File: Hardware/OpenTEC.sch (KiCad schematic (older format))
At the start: 65 parts, among them J10 TEMP3, J11 TEC, J12 XH2.54, J13 XH2.54, J14 XH2.54, J15 XH2.54, J16 XH2.54, J17 XH2.54, J18 XH2.54, J19 XH2.54, J2 4P Screw Terminal, J20 XH2.54, J21 XH2.54, J22 XH2.54, J23 XH2.54, J24 XH2.54, J25 XH2.54, J26 XH2.54, J27 XH2.54, J3 10P JTAG/SWD, J4 LCD, J5 I2C, J6 BOOT_SEL, J7 TEMP0, J8 TEMP1, J9 TEMP2, Q1 FDS6574A, Q2 FDS6574A, Q3 FDS6574A, Q4 FDS6574A, U11 STM32F103C8T6, U2 AMS1117-3.3, U3 IR2104, U4 IR2104, Y1 16MHz

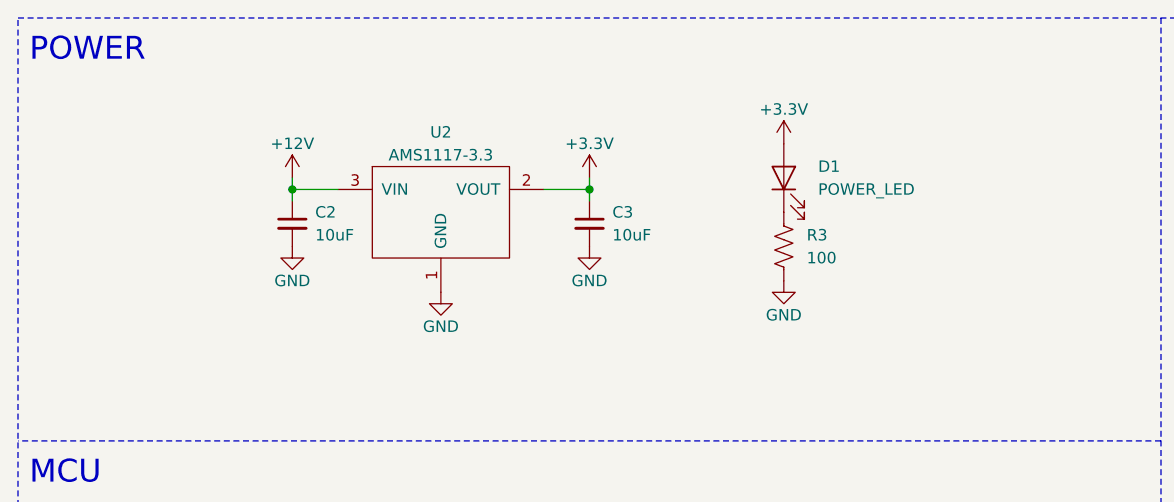
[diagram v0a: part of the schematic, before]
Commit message: Add RC filter to 3.3V LDO input
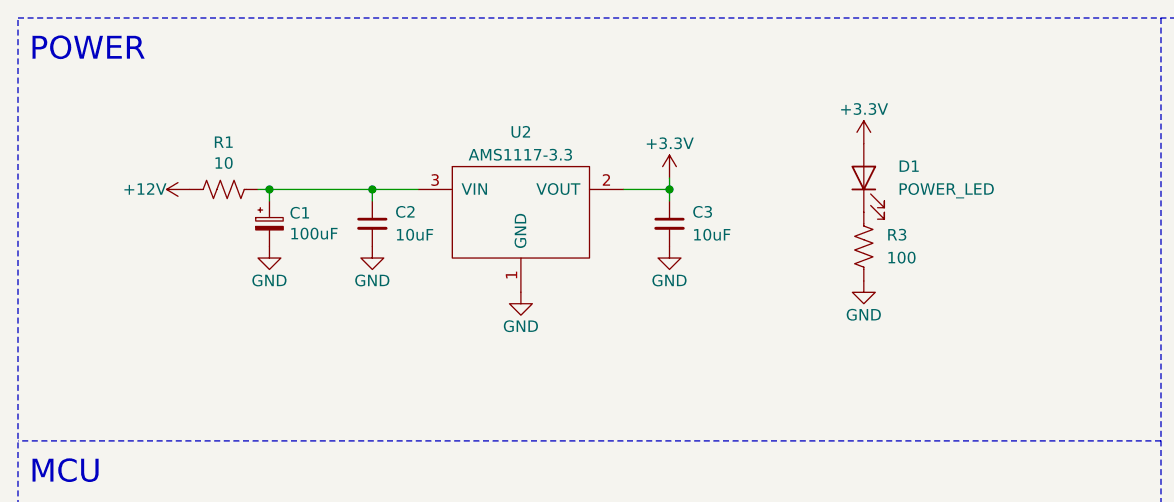
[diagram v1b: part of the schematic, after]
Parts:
- added C1: 100uF, Capacitor_SMD:CP_Elec_6.3x5.8, symbol Device:CP_Small
- added R1: 10, Resistor_THT:R_Axial_Power_L20.0mm_W6.4mm_P22.40mm, symbol Device:R_US
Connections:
- net +12V: now also R1.2; no longer C2.1, U2.3 (VIN)
- net GND: now also C1.2
- new net: C1.1, C2.1, R1.1, U2.3 (VIN)
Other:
- moved on the sheet: C2, C3, D1, R3, U2
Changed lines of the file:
@@
 L power:+3.3V #PWR03
 U 1 1 6014EE85
-P 3850 1050
-F 0 "#PWR03" H 3850 900 50  0001 C CNN
-F 1 "+3.3V" H 3850 1200 50  0000 C CNN
-F 2 "" H 3850 1050 50  0001 C CNN
-F 3 "" H 3850 1050 50  0001 C CNN
-	1    3850 1050
+P 4200 1050
+F 0 "#PWR03" H 4200 900 50  0001 C CNN
+F 1 "+3.3V" H 4200 1200 50  0000 C CNN
+F 2 "" H 4200 1050 50  0001 C CNN
+F 3 "" H 4200 1050 50  0001 C CNN
+	1    4200 1050
 	1    0    0    -1
 $EndComp
@@
 L power:GND #PWR012
 U 1 1 6014DF95
-P 3850 1650
-F 0 "#PWR012" H 3850 1400 50  0001 C CNN
-F 1 "GND" H 3850 1500 50  0000 C CNN
-F 2 "" H 3850 1650 50  0001 C CNN
-F 3 "" H 3850 1650 50  0001 C CNN
-	1    3850 1650
+P 4200 1650
+F 0 "#PWR012" H 4200 1400 50  0001 C CNN
+F 1 "GND" H 4200 1500 50  0000 C CNN
+F 2 "" H 4200 1650 50  0001 C CNN
+F 3 "" H 4200 1650 50  0001 C CNN
+	1    4200 1650
 	1    0    0    -1
 $EndComp
@@
 L Device:R_US R3
 U 1 1 6014CE76
-P 3850 1500
-F 0 "R3" H 3950 1550 50  0000 L CNN
-F 1 "100" H 3950 1450 50  0000 L CNN
-F 2 "Resistor_SMD:R_0402_1005Metric" V 3890 1490 50  0001 C CNN
-F 3 "~" H 3850 1500 50  0001 C CNN
-	1    3850 1500
+P 4200 1500
+F 0 "R3" H 4300 1550 50  0000 L CNN
+F 1 "100" H 4300 1450 50  0000 L CNN
+F 2 "Resistor_SMD:R_0402_1005Metric" V 4240 1490 50  0001 C CNN
+F 3 "~" H 4200 1500 50  0001 C CNN
+	1    4200 1500
 	1    0    0    -1
 $EndComp
@@
 L Device:LED D1
 U 1 1 6014BC21
-P 3850 1200
-F 0 "D1" V 3900 1050 50  0000 R CNN
-F 1 "POWER_LED" V 3800 1050 50  0000 R CNN
-F 2 "LED_SMD:LED_0603_1608Metric" H 3850 1200 50  0001 C CNN
-F 3 "~" H 3850 1200 50  0001 C CNN
-	1    3850 1200
+P 4200 1200
+F 0 "D1" V 4250 1050 50  0000 R CNN
+F 1 "POWER_LED" V 4150 1050 50  0000 R CNN
+F 2 "LED_SMD:LED_0603_1608Metric" H 4200 1200 50  0001 C CNN
+F 3 "~" H 4200 1200 50  0001 C CNN
+	1    4200 1200
 	0    -1   -1   0
 $EndComp
-Wire Wire Line
-	1700 1200 1700 1250
-Connection ~ 3000 1250
-Wire Wire Line
-	3000 1200 3000 1250
-$Comp
-L power:+12V #PWR06
-U 1 1 6012AA6B
-P 1700 1200
-F 0 "#PWR06" H 1700 1050 50  0001 C CNN
-F 1 "+12V" H 1700 1350 50  0000 C CNN
-F 2 "" H 1700 1200 50  0001 C CNN
-F 3 "" H 1700 1200 50  0001 C CNN
-	1    1700 1200
-	1    0    0    -1
-$EndComp
+Connection ~ 3350 1250
+Wire Wire Line
+	3350 1200 3350 1250
 $Comp
 L power:+3.3V #PWR08
 U 1 1 601276ED
-P 3000 1200
-F 0 "#PWR08" H 3000 1050 50  0001 C CNN
-F 1 "+3.3V" H 3000 1350 50  0000 C CNN
-F 2 "" H 3000 1200 50  0001 C CNN
-F 3 "" H 3000 1200 50  0001 C CNN
-	1    3000 1200
+P 3350 1200
+F 0 "#PWR08" H 3350 1050 50  0001 C CNN
+F 1 "+3.3V" H 3350 1350 50  0000 C CNN
+F 2 "" H 3350 1200 50  0001 C CNN
+F 3 "" H 3350 1200 50  0001 C CNN
+	1    3350 1200
 	1    0    0    -1
 $EndComp
@@
 L power:GND #PWR014
 U 1 1 601272FB
-P 2350 1700
-F 0 "#PWR014" H 2350 1450 50  0001 C CNN
-F 1 "GND" H 2350 1550 50  0000 C CNN
-F 2 "" H 2350 1700 50  0001 C CNN
-F 3 "" H 2350 1700 50  0001 C CNN
-	1    2350 1700
-	1    0    0    -1
-$EndComp
-Wire Wire Line
-	3000 1250 3000 1300
-Wire Wire Line
-	2800 1250 3000 1250
-Wire Wire Line
-	1700 1250 1900 1250
-Connection ~ 1700 1250
-Wire Wire Line
-	1700 1300 1700 1250
+P 2700 1700
+F 0 "#PWR014" H 2700 1450 50  0001 C CNN
+F 1 "GND" H 2700 1550 50  0000 C CNN
+F 2 "" H 2700 1700 50  0001 C CNN
+F 3 "" H 2700 1700 50  0001 C CNN
+	1    2700 1700
+	1    0    0    -1
+$EndComp
+Wire Wire Line
+	3350 1250 3350 1300
+Wire Wire Line
+	3150 1250 3350 1250
+Wire Wire Line
+	2050 1250 2250 1250
+Wire Wire Line
+	2050 1300 2050 1250
 $Comp
 L power:GND #PWR011
 U 1 1 6012585B
-P 3000 1500
-F 0 "#PWR011" H 3000 1250 50  0001 C CNN
-F 1 "GND" H 3000 1350 50  0000 C CNN
-F 2 "" H 3000 1500 50  0001 C CNN
-F 3 "" H 3000 1500 50  0001 C CNN
-	1    3000 1500
+P 3350 1500
+F 0 "#PWR011" H 3350 1250 50  0001 C CNN
+F 1 "GND" H 3350 1350 50  0000 C CNN
+F 2 "" H 3350 1500 50  0001 C CNN
+F 3 "" H 3350 1500 50  0001 C CNN
+	1    3350 1500
 	1    0    0    -1
 $EndComp
@@
 L Device:C_Small C3
 U 1 1 60125855
-P 3000 1400
-F 0 "C3" H 3100 1450 50  0000 L CNN
-F 1 "10uF" H 3100 1350 50  0000 L CNN
-F 2 "Capacitor_SMD:C_0805_2012Metric" H 3000 1400 50  0001 C CNN
-F 3 "~" H 3000 1400 50  0001 C CNN
-	1    3000 1400
+P 3350 1400
+F 0 "C3" H 3450 1450 50  0000 L CNN
+F 1 "10uF" H 3450 1350 50  0000 L CNN
+F 2 "Capacitor_SMD:C_0805_2012Metric" H 3350 1400 50  0001 C CNN
+F 3 "~" H 3350 1400 50  0001 C CNN
+	1    3350 1400
 	1    0    0    -1
 $EndComp
@@
 L power:GND #PWR010
 U 1 1 6012438B
-P 1700 1500
-F 0 "#PWR010" H 1700 1250 50  0001 C CNN
-F 1 "GND" H 1700 1350 50  0000 C CNN
-F 2 "" H 1700 1500 50  0001 C CNN
-F 3 "" H 1700 1500 50  0001 C CNN
-	1    1700 1500
+P 2050 1500
+F 0 "#PWR010" H 2050 1250 50  0001 C CNN
+F 1 "GND" H 2050 1350 50  0000 C CNN
+F 2 "" H 2050 1500 50  0001 C CNN
+F 3 "" H 2050 1500 50  0001 C CNN
+	1    2050 1500
 	1    0    0    -1
 $EndComp
@@
 L Device:C_Small C2
 U 1 1 60124385
-P 1700 1400
-F 0 "C2" H 1800 1450 50  0000 L CNN
-F 1 "10uF" H 1800 1350 50  0000 L CNN
-F 2 "Capacitor_SMD:C_0805_2012Metric" H 1700 1400 50  0001 C CNN
-F 3 "~" H 1700 1400 50  0001 C CNN
-	1    1700 1400
+P 2050 1400
+F 0 "C2" H 2150 1450 50  0000 L CNN
+F 1 "10uF" H 2150 1350 50  0000 L CNN
+F 2 "Capacitor_SMD:C_0805_2012Metric" H 2050 1400 50  0001 C CNN
+F 3 "~" H 2050 1400 50  0001 C CNN
+	1    2050 1400
 	1    0    0    -1
 $EndComp
@@
 L OpenTEC:AMS1117 U2
 U 1 1 6011CBE4
-P 2350 1300
-F 0 "U2" H 2350 1600 50  0000 C CNN
-F 1 "AMS1117-3.3" H 2350 1500 50  0000 C CNN
-F 2 "Package_TO_SOT_SMD:SOT-223-3_TabPin2" H 2350 1600 50  0001 C CNN
-F 3 "" H 2350 1600 50  0001 C CNN
-	1    2350 1300
+P 2700 1300
+F 0 "U2" H 2700 1600 50  0000 C CNN
+F 1 "AMS1117-3.3" H 2700 1500 50  0000 C CNN
+F 2 "Package_TO_SOT_SMD:SOT-223-3_TabPin2" H 2700 1600 50  0001 C CNN
+F 3 "" H 2700 1600 50  0001 C CNN
+	1    2700 1300
 	1    0    0    -1
 $EndComp
@@
 NoConn ~ 2650 6250
 NoConn ~ 2650 6350
+$Comp
+L Device:R_US R1
+U 1 1 601B9489
+P 1400 1250
+F 0 "R1" V 1195 1250 50  0000 C CNN
+F 1 "10" V 1286 1250 50  0000 C CNN
+F 2 "Resistor_THT:R_Axial_Power_L20.0mm_W6.4mm_P22.40mm" V 1440 1240 50  0001 C CNN
+F 3 "~" H 1400 1250 50  0001 C CNN
+	1    1400 1250
+	0    1    1    0
+$EndComp
+$Comp
+L power:+12V #PWR02
+U 1 1 601BC96C
+P 1250 1250
+F 0 "#PWR02" H 1250 1100 50  0001 C CNN
+F 1 "+12V" V 1250 1350 50  0000 L CNN
+F 2 "" H 1250 1250 50  0001 C CNN
+F 3 "" H 1250 1250 50  0001 C CNN
+	1    1250 1250
+	0    -1   -1   0
+$EndComp
+$Comp
+L power:GND #PWR05
+U 1 1 601C1543
+P 1600 1500
+F 0 "#PWR05" H 1600 1250 50  0001 C CNN
+F 1 "GND" H 1600 1350 50  0000 C CNN
+F 2 "" H 1600 1500 50  0001 C CNN
+F 3 "" H 1600 1500 50  0001 C CNN
+	1    1600 1500
+	1    0    0    -1
+$EndComp
+$Comp
+L Device:CP_Small C1
+U 1 1 601C37E4
+P 1600 1400
+F 0 "C1" H 1688 1446 50  0000 L CNN
+F 1 "100uF" H 1688 1355 50  0000 L CNN
+F 2 "Capacitor_SMD:CP_Elec_6.3x5.8" H 1600 1400 50  0001 C CNN
+F 3 "~" H 1600 1400 50  0001 C CNN
+	1    1600 1400
+	1    0    0    -1
+$EndComp
+Wire Wire Line
+	1600 1250 1550 1250
+Wire Wire Line
+	1600 1250 1600 1300
+Connection ~ 1600 1250
+Wire Wire Line
+	1600 1250 2050 1250
+Connection ~ 2050 1250
 $EndSCHEMATC

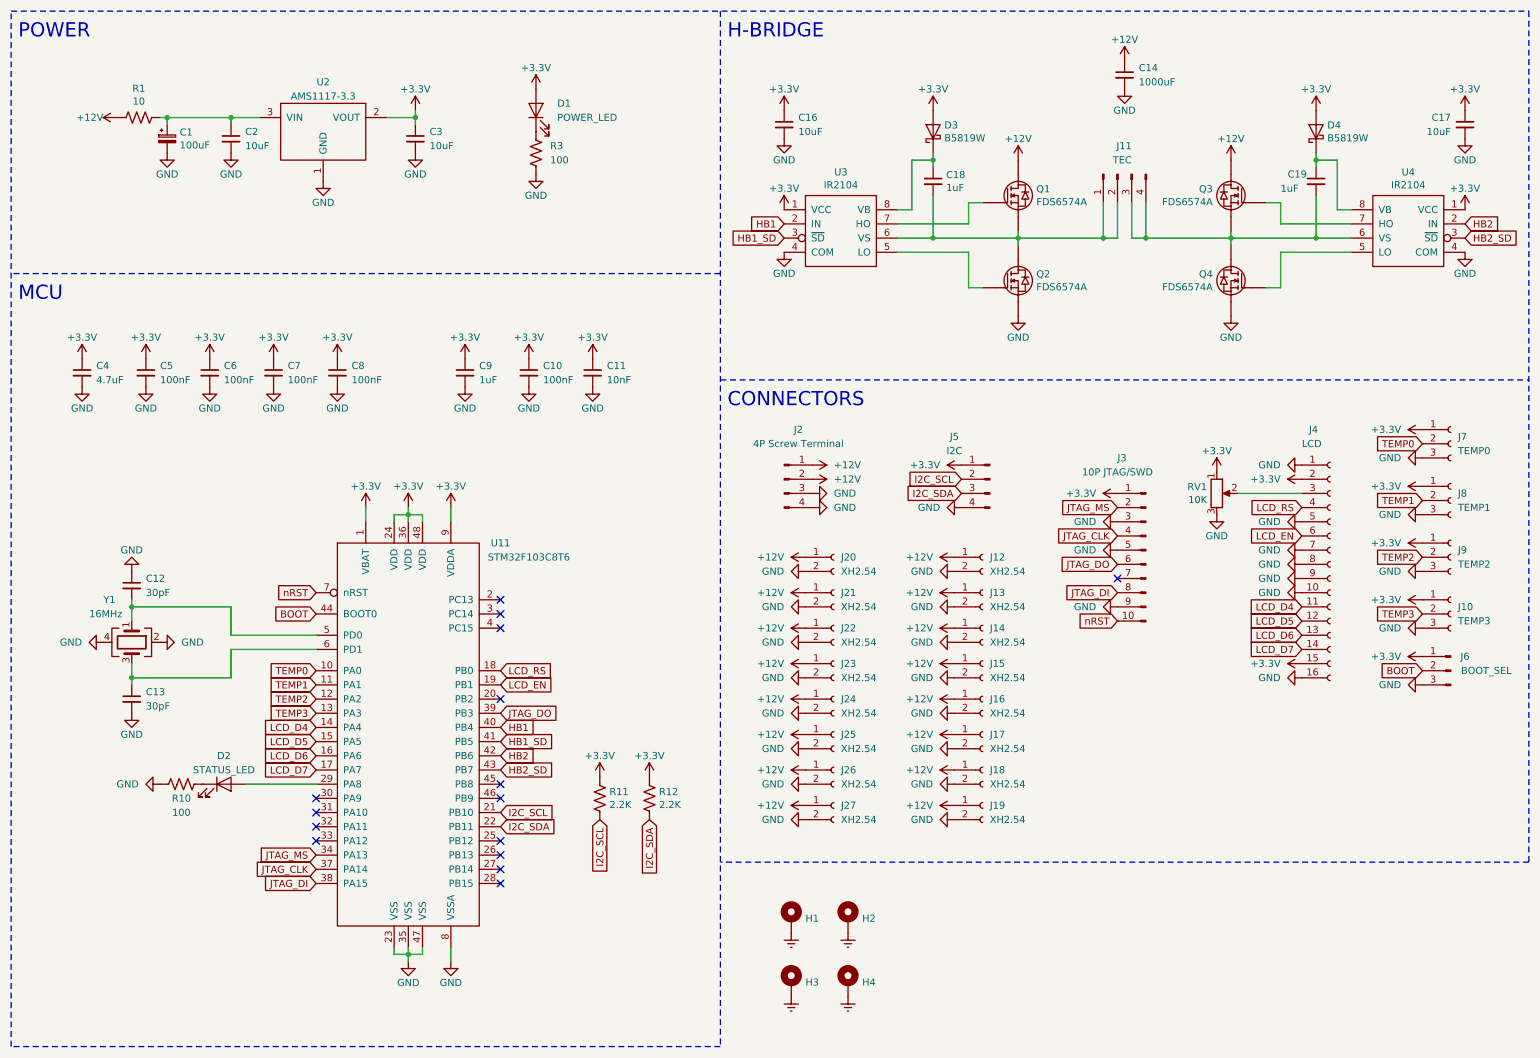
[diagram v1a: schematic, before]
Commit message: Add control push buttons
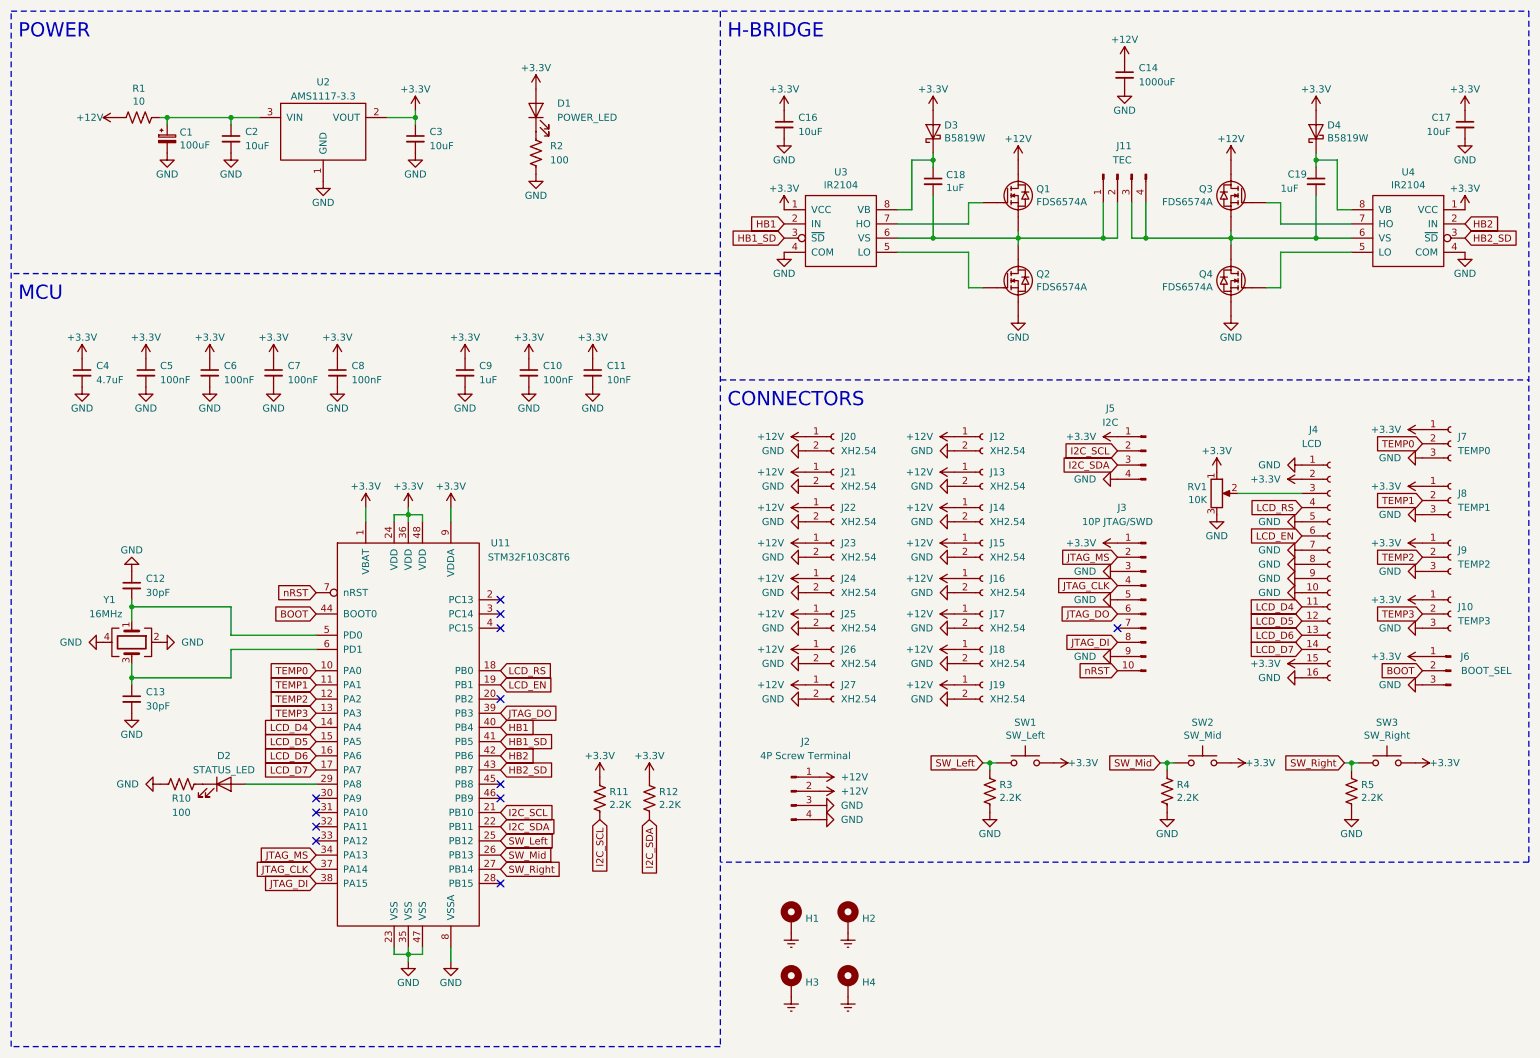
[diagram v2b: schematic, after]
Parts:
- added R3, R4, R5: 2.2K, Resistor_SMD:R_0402_1005Metric, symbol Device:R_US
- added SW1: SW_Left, Button_Switch_THT:SW_PUSH_6mm, symbol Switch:SW_Push
- added SW2: SW_Mid, Button_Switch_THT:SW_PUSH_6mm, symbol Switch:SW_Push
- added SW3: SW_Right, Button_Switch_THT:SW_PUSH_6mm, symbol Switch:SW_Push
- renumbered R3 to R2
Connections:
- net +3V3: now also SW1.2, SW2.2, SW3.2
- net GND: now also R3.2, R4.2, R5.2
- net SW_Left: now reaches U11.25 (PB12)
- net SW_Left: now also R3.1, SW1.1
- net SW_Mid: now reaches U11.26 (PB13)
- net SW_Mid: now also R4.1, SW2.1
- net SW_Right: now reaches U11.27 (PB14)
- net SW_Right: now also R5.1, SW3.1
- no-connect marks 15 -> 12
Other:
- moved on the sheet: J12, J13, J14, J15, J16, J17, J18, J19, J2, J20, J21, J22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

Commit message: Fix H-bridge supply voltage
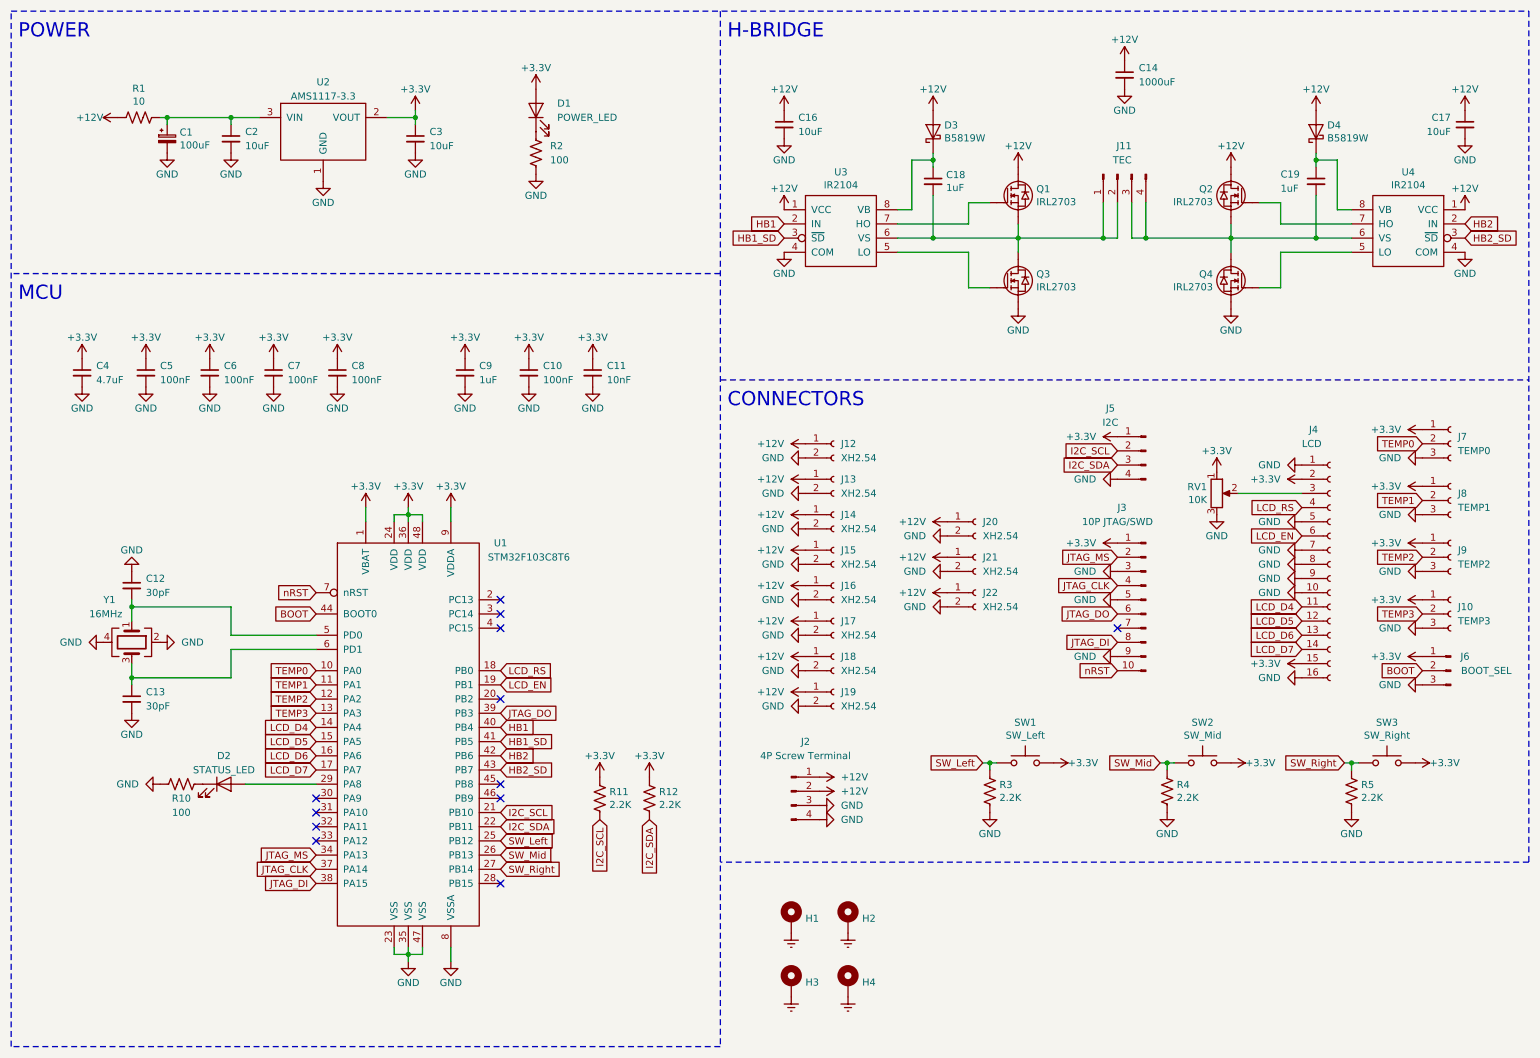
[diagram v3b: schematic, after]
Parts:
- removed J23, J24, J25, J26, J27: XH2.54, Connector_JST:JST_XH_B2B-XH-A_1x02_P2.50mm_Vertical, symbol Connector:Conn_01x02_Female
- removed Q1, Q2, Q3, Q4: FDS6574A, Package_SO:SOIC-8_3.9x4.9mm_P1.27mm, symbol OpenTEC:FDS6574A
- added Q1, Q2, Q3, Q4: IRL2703, Package_TO_SOT_THT:TO-220-3_Vertical, symbol OpenTEC:IRL2703
- C1: footprint Capacitor_SMD:CP_Elec_6.3x5.8 -> Capacitor_SMD:CP_Elec_6.3x5.3
- renumbered U11 to U1
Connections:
- net +12V: now also C16.1, C17.1, D3.2 (A), D4.2 (A), U3.1 (VCC), U4.1 (VCC), Q1.2, Q2.2
- net +3V3: no longer C16.1, C17.1, D3.2 (A), D4.2 (A), U3.1 (VCC), U4.1 (VCC)
- net GND: now also Q3.3, Q4.3
- net at C18.2, J11.1 (Pin_1), J11.2 (Pin_2)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: now also Q1.3, Q3.2
- net at U3.7 (HO): now also Q1.1
- net at U3.5 (LO): now also Q3.1
- net at C19.2, J11.3 (Pin_3), J11.4 (Pin_4)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: now also Q2.3, Q4.2
- net at U4.7 (HO): now also Q2.1
- net at U4.5 (LO): now also Q4.1
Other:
- moved on the sheet: J12, J13, J14, J15, J16, J17, J18, J19, J20, J21, J22
